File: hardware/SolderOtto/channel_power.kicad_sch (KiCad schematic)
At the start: 20 parts, among them Q801 Q_Dual_NMOS, Q802 Q_Dual_NMOS, Q803 Q_Dual_NMOS, Q804 DTD123EK, Q805 DTD123EK, Q806 DTD123EK, Q807 Q_Dual_NMOS, Q808 Q_Dual_NMOS, Q809 DTD123EK, Q810 DTD123EK, U801 VOM1271, U802 VOM1271, U803 VOM1271, U804 VOM1271, U805 VOM1271

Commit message: save wip
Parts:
- renumbered Q801 to Q701, Q802 to Q702, Q803 to Q703, Q804 to Q704, Q805 to Q705, Q806 to Q706, Q807 to Q707, Q808 to Q708, Q809 to Q709, Q810 to Q710, R801 to R701, R802 to R702, R803 to R703, R804 to R704, R805 to R705, U801 to U701, U802 to U702, U803 to U703, U804 to U704, U805 to U705

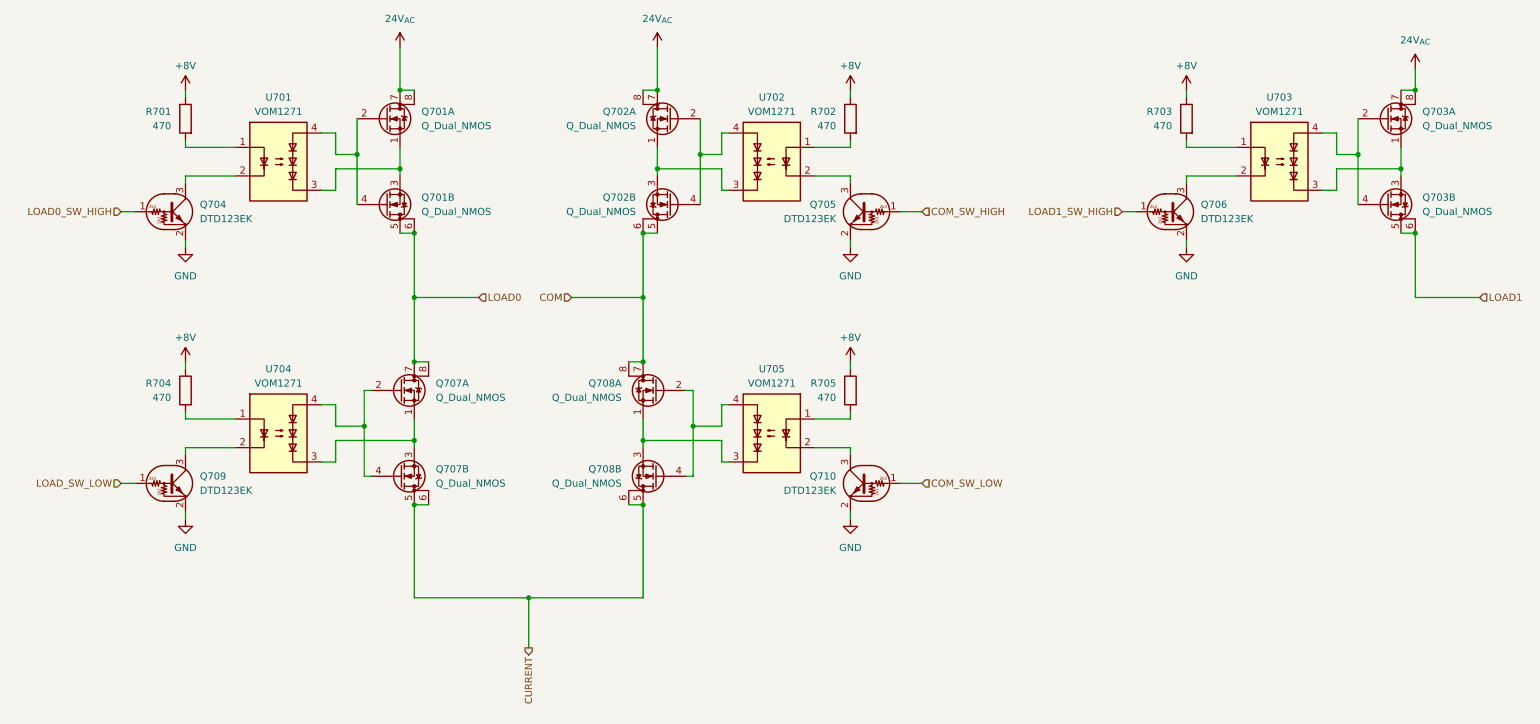
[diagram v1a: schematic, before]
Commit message: rework schematic foir single channel
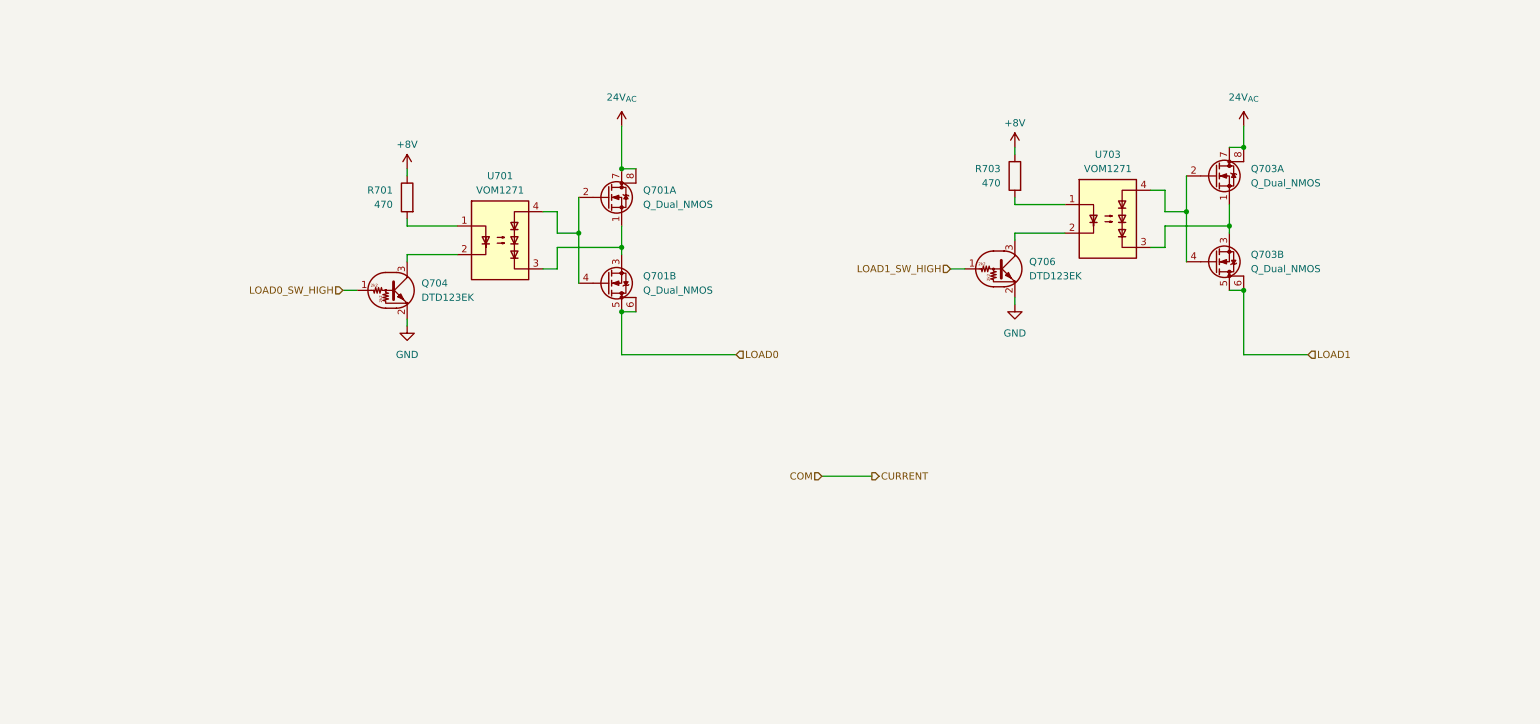
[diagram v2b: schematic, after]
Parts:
- removed Q702, Q707, Q708: Q_Dual_NMOS, Package_SO:SO-8_3.9x4.9mm_P1.27mm, symbol Device:Q_Dual_NMOS_S1G1S2G2D2D2D1D1
- removed Q705, Q709, Q710: DTD123EK, Package_TO_SOT_SMD:SC-59, symbol Transistor_BJT:DTD123E
- removed R702, R704, R705: 470, Resistor_SMD:R_0603_1608Metric, symbol Device:R
- removed U702, U704, U705: VOM1271, mylib_ic:SOP-4_3.8x4.1mm_P2.54mm, symbol mylib_diodes:VOM1271
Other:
- moved on the sheet: Q701A, Q701B, Q703A, Q703B, Q704, Q706, R701, R703, U701, U703
